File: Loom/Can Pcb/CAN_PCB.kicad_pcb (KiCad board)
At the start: 2 copper layers, 129.5 x 58.4 mm, 40 parts, among them J1 Conn_01x03, J12 Conn_01x03, J13 Conn_01x03, J14 Conn_01x03, J15 Conn_01x03, J16 Conn_01x03, J17 Conn_01x03, J2 Conn_01x05_Pin, J3 Screw_Terminal_01x02, J4 Conn_01x02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

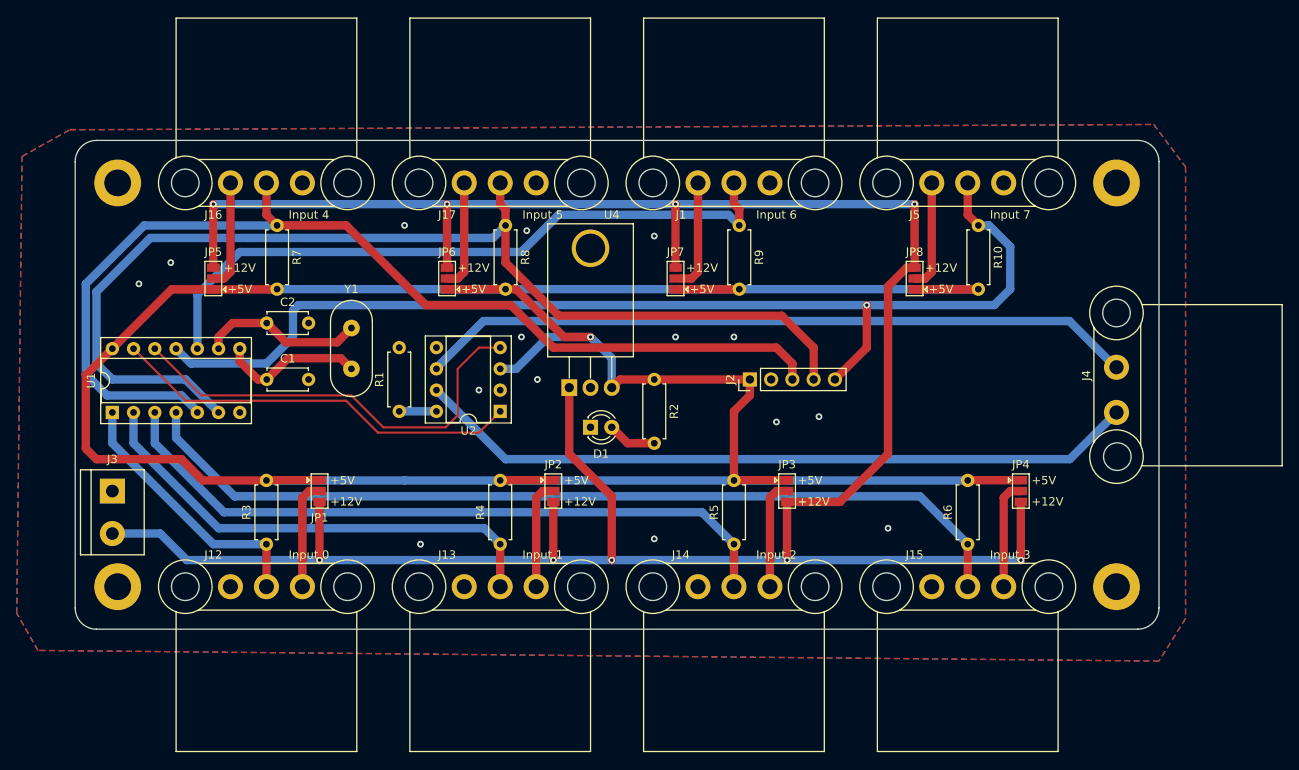
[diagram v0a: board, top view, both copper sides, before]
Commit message: Made changes to can pcb layout
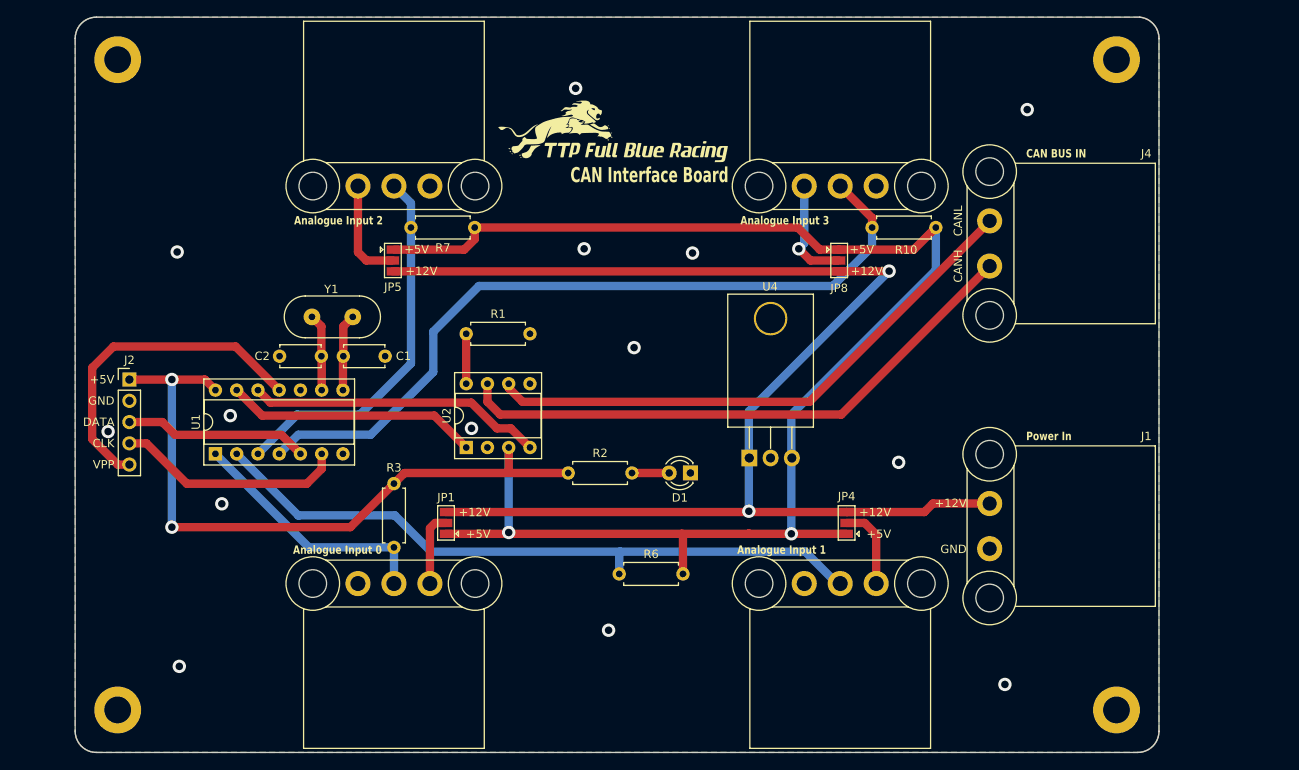
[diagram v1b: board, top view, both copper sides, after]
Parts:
- removed the ? at (97.8, 63.5)
- removed the ? at (217.2, 63.5)
- removed the ? at (217.2, 111.8)
- removed the ? at (97.8, 111.8)
- removed J13, J14, J17: Conn_01x03, BSPD_footprints:ATF13-3P-BM03
- removed J3: Screw_Terminal_01x02, TerminalBlock:TerminalBlock_bornier-2_P5.08mm
- removed JP2, JP3, JP6, JP7: SolderJumper_3_Open, Jumper:SolderJumper-3_P1.3mm_Open_Pad1.0x1.5mm
- removed R4, R5, R8, R9: 5Meg, Resistor_THT:R_Axial_DIN0207_L6.3mm_D2.5mm_P7.62mm_Horizontal
- added ?: , , F.Cu at (97.8, 48.8)
- added ?: , , F.Cu at (97.8, 126.5)
- added ?: , , F.Cu at (217.2, 48.8)
- added ?: , , F.Cu at (217.2, 126.5)
- added G***: LOGO, LOGO, F.Cu at (157.0, 56.6)
- J1: value Conn_01x03 -> Conn_01x02; footprint BSPD_footprints:ATF13-3P-BM03 -> Footprints:ATF13-2P-BM03
- moved J2 74.2 mm to (99.2, 87.0), turned to 0 degrees
- moved J1 51.0 mm to (202.0, 107.2), turned to 90 degrees
- moved R6 41.8 mm to (157.7, 110.2), turned to 0 degrees
- moved J4 23.1 mm to (202.0, 73.4)
- moved U4 23.1 mm to (173.2, 96.5)
- moved JP5 21.6 mm to (130.7, 72.8), turned to -90 degrees
- moved JP4 21.2 mm to (184.9, 104.1), turned to 90 degrees
- moved R7 16.0 mm to (132.8, 68.8), turned to 0 degrees
- moved JP1 15.6 mm to (137.0, 104.1), turned to 90 degrees
- moved R3 15.2 mm to (130.8, 107.1)
- moved J12 15.2 mm to (126.5, 111.4)
- moved J15 15.2 mm to (179.8, 111.4)
- moved J16 15.2 mm to (135.1, 63.9)
- moved J5 15.2 mm to (188.4, 63.9)
- moved R2 15.2 mm to (151.6, 98.2), turned to 0 degrees
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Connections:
- net /AN5 renamed /CLK
- J1 pad 2: /AN6 -> +12V
- J15 pad 2: /AN3 -> /AN1
- J16 pad 2: /AN4 -> /AN2
- J2 pad 3: /AN4 -> /DATA
- J2 pad 5: /AN7 -> /VPP
- J5 pad 2: /AN7 -> /AN3
- R10 pad 1: /AN7 -> /AN3
- R6 pad 1: /AN3 -> /AN1
- R7 pad 1: /AN4 -> /AN2
- U1 pad 10: /AN6 -> unconnected-(U1-GP6-Pad10)
- U1 pad 11: /AN7 -> /VPP
- U1 pad 5: /AN4 -> /DATA
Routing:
- net +12V: track 313.2 -> 160.3 mm, vias 9 -> 2
- net /AN7: track 132.0 -> 0.00 mm, vias 1 -> 0
- net /AN4: track 127.8 -> 0.00 mm
- net /CLK: track 132.4 -> 27.5 mm
- net /AN6: track 80.9 -> 0.00 mm
- net +5V: track 335.9 -> 256.5 mm, vias 1 -> 4
- net /VPP: track 0.00 -> 39.8 mm
- net /AN2: track 83.0 -> 44.8 mm
- net /AN1: track 57.6 -> 81.4 mm
- net /DATA: track 0.00 -> 22.0 mm
- net /TXCAN: track 49.0 -> 30.3 mm
- net Net-(J4-Pin_2): track 85.9 -> 67.7 mm
- net /RXCAN: track 52.4 -> 35.4 mm
- net Net-(J4-Pin_1): track 87.0 -> 70.2 mm
- net /AN3: track 108.0 -> 93.2 mm
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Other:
- board size 129.5 x 58.4 mm -> 129.5 x 87.9 mm
- board text added: "Analogue Input 0"
- board text added: "Analogue Input 1"
- board text added: "Analogue Input 2"
- board text added: "Analogue Input 3"
- board text added: "CAN BUS IN"
- board text added: "CAN Interface Board"
- board text added: "CANH"
- board text added: "CANL"
- board text added: "CLK"
- board text added: "DATA"
- board text added: "GND"
- board text added: "Power In"
- board text added: "VPP"
- board text removed: "Input 0"
- board text removed: "Input 1"
- board text removed: "Input 2"
- board text removed: "Input 3"
- board text removed: "Input 4"
- board text removed: "Input 5"
- board text removed: "Input 6"
- board text removed: "Input 7"
